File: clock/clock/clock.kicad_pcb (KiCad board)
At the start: 2 copper layers, 32.3 x 110 mm, 44 parts, among them J1 AVR-ISP, J10 Conn_01x07_Male, J11 CV_IN, J12 CLOCK_OUT, J13 SUBDIV_OUT, J2 EURORACK_CONN_10, J3 Conn_01x05_Female, J4 Conn_01x05_Male, J5 Conn_01x05_Female, J6 Conn_01x05_Male, J7 Conn_01x05_Female, J8 Conn_01x05_Male, J9 Conn_01x07_Female, SW1 SW_Push, SW2 SW_Push, SW3 Rotary_Encoder_Switch, U1 ATmega328P-PU, U2 L7805, U3 SM460281N, U4 SM460281N, U5 SM460281N, Y1 16MHz

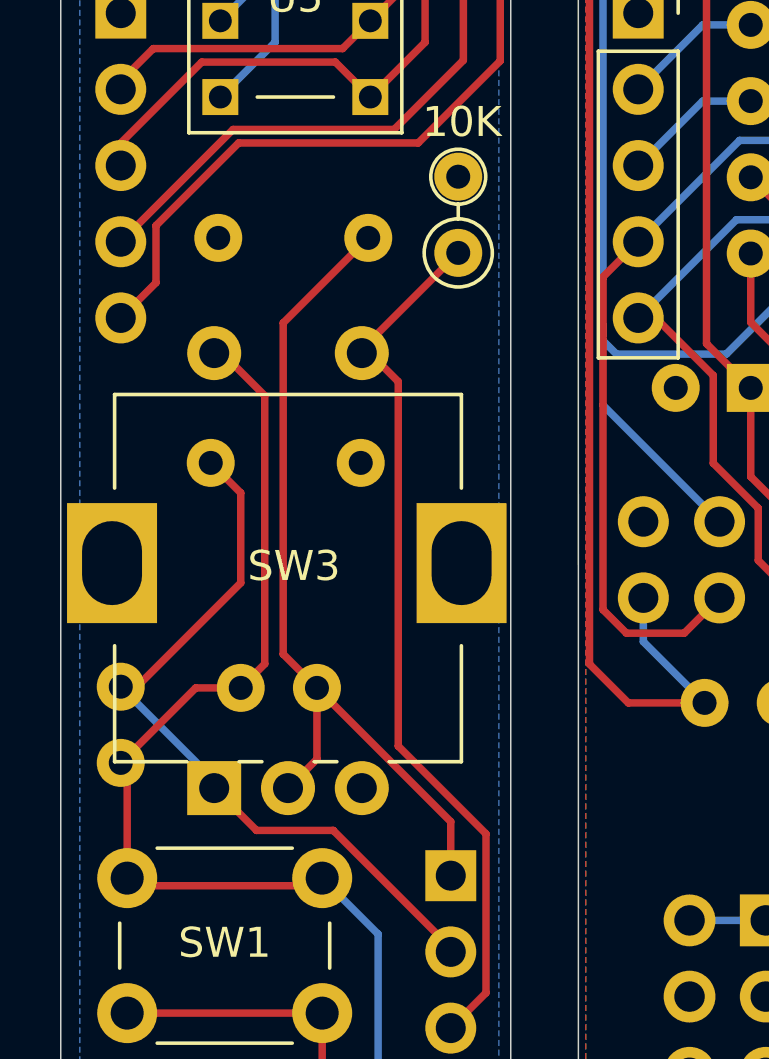
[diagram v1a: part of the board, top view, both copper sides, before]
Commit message: fix some PCB bugs
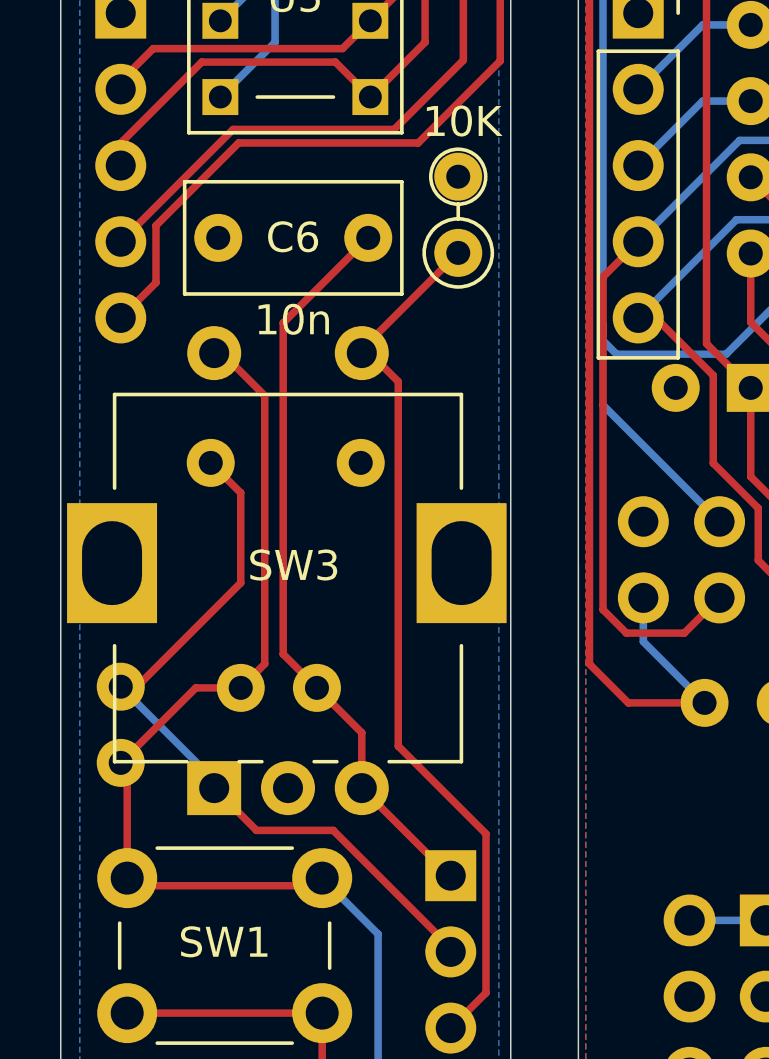
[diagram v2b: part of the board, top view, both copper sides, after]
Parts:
- C6: moved to F.Cu
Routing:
- net /KNOBR: track 28.5 -> 24.8 mm
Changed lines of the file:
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@@
+    )
+  )
+  (footprint "Capacitor_THT:C_Rect_L7.0mm_W3.5mm_P5.00mm" (layer "F.Cu")
+    (at 110.075 124.06 180)
+    (descr "C, Rect series, Radial, pin pitch=5.00mm, , length*width=7*3.5mm^2, Capacitor")
+    (tags "C Rect series Radial pin pitch 5.00mm  length 7mm width 3.5mm Capacitor")
+    (property "Sheetfile" "clock.kicad_sch")
+    (property "Sheetname" "")
+    (attr through_hole)
+    (fp_text reference "C6" (at 2.5 0) (layer "F.SilkS")
+      (effects (font (size 1 1) (thickness 0.15)))
+    )
+    (fp_text value "10n" (at 2.5 -2.75) (layer "F.SilkS")
+      (effects (font (size 1 1) (thickness 0.15)))
+    )
+    (fp_text user "${REFERENCE}" (at 2.5 0) (layer "F.Fab")
+      (effects (font (size 1 1) (thickness 0.15)))
+    )
+    (fp_line (start -1.12 -1.87) (end -1.12 1.87) (layer "F.SilkS") (width 0.12))
+    (fp_line (start -1.12 -1.87) (end 6.12 -1.87) (layer "F.SilkS") (width 0.12))
+    (fp_line (start -1.12 1.87) (end 6.12 1.87) (layer "F.SilkS") (width 0.12))
+    (fp_line (start 6.12 -1.87) (end 6.12 1.87) (layer "F.SilkS") (width 0.12))
+    (fp_line (start 6.25 -2) (end -1.25 -2) (layer "F.CrtYd") (width 0.05))
+    (fp_line (start -1.25 2) (end 6.25 2) (layer "F.CrtYd") (width 0.05))
+    (fp_line (start -1.25 -2) (end -1.25 2) (layer "F.CrtYd") (width 0.05))
+    (fp_line (start 6.25 2) (end 6.25 -2) (layer "F.CrtYd") (width 0.05))
+    (fp_line (start -1 -1.75) (end -1 1.75) (layer "F.Fab") (width 0.1))
+    (fp_line (start 6 1.75) (end 6 -1.75) (layer "F.Fab") (width 0.1))
+    (fp_line (start 6 -1.75) (end -1 -1.75) (layer "F.Fab") (width 0.1))
+    (fp_line (start -1 1.75) (end 6 1.75) (layer "F.Fab") (width 0.1))
+    (pad "1" thru_hole circle locked (at 0 0 180) (size 1.6 1.6) (drill 0.8) (layers *.Cu *.Mask)
+      (net 54 "/KNOBR") (pintype "passive"))
+    (pad "2" thru_hole circle locked (at 5 0 180) (size 1.6 1.6) (drill 0.8) (layers *.Cu *.Mask)
+      (net 25 "/AGND") (pintype "passive"))
+    (model "${KISYS3DMOD}/Capacitor_THT.3dshapes/C_Rect_L7.0mm_W3.5mm_P5.00mm.wrl"
+      (offset (xyz 0 0 0))
+      (scale (xyz 1 1 1))
+      (rotate (xyz 0 0 0))
     )
   )
@@
       (effects (font (size 1 1) (thickness 0.15)))
     )
+    (fp_line (start 10 3.28) (end 13.12 3.28) (layer "F.SilkS") (width 0.12))
+    (fp_line (start 10 -8.28) (end 13.12 -8.28) (layer "F.SilkS") (width 0.12))
     (fp_line (start 0.88 -4.129) (end 0.88 -3.37) (layer "F.SilkS") (width 0.12))
-    (fp_line (start 10 3.28) (end 13.12 3.28) (layer "F.SilkS") (width 0.12))
+    (fp_line (start 0.88 -8.28) (end 4.745 -8.28) (layer "F.SilkS") (width 0.12))
     (fp_line (start 13.12 -8.28) (end 13.12 3.28) (layer "F.SilkS") (width 0.12))
     (fp_line (start 0.88 -1.629) (end 0.88 -0.87) (layer "F.SilkS") (width 0.12))
-    (fp_line (start 10 -8.28) (end 13.12 -8.28) (layer "F.SilkS") (width 0.12))
-    (fp_line (start 0.88 -8.28) (end 0.88 -5.871) (layer "F.SilkS") (width 0.12))
-    (fp_line (start 0.88 -8.28) (end 4.745 -8.28) (layer "F.SilkS") (width 0.12))
     (fp_line (start 0.88 0.87) (end 0.88 3.28) (layer "F.SilkS") (width 0.12))
     (fp_line (start 0.88 3.28) (end 4.745 3.28) (layer "F.SilkS") (width 0.12))
+    (fp_line (start 0.88 -8.28) (end 0.88 -5.871) (layer "F.SilkS") (width 0.12))
     (fp_line (start 15.65 4.8) (end 15.65 -9.9) (layer "F.CrtYd") (width 0.05))
     (fp_line (start 15.65 -9.9) (end -1.15 -9.9) (layer "F.CrtYd") (width 0.05))
@@
     (fp_line (start -1.15 -9.9) (end -1.15 4.8) (layer "F.CrtYd") (width 0.05))
     (fp_line (start 13 3.87) (end 13 -8.87) (layer "F.Fab") (width 0.1))
+    (fp_line (start 1 3.87) (end 13 3.87) (layer "F.Fab") (width 0.1))
+    (fp_line (start 1 -8.87) (end 1 3.87) (layer "F.Fab") (width 0.1))
     (fp_line (start 13 -8.87) (end 1 -8.87) (layer "F.Fab") (width 0.1))
-    (fp_line (start 1 -8.87) (end 1 3.87) (layer "F.Fab") (width 0.1))
-    (fp_line (start 1 3.87) (end 13 3.87) (layer "F.Fab") (width 0.1))
     (fp_circle (center 7.5 -2.5) (end 10.5 -2.5) (layer "F.Fab") (width 0.1) (fill none))
     (pad "" thru_hole rect (at 7.5 3.285 90) (size 4 3) (drill oval 2.8 2) (layers *.Cu *.Mask))
@@
     (pad "1" thru_hole rect (at 0 -4.96 90) (size 1.8 1.8) (drill 1) (layers *.Cu *.Mask)
       (net 55 "/KNOBL") (pinfunction "A") (pintype "passive"))
-    (pad "2" thru_hole circle (at 0 -2.5 90) (size 1.8 1.8) (drill 1) (layers *.Cu *.Mask)
+    (pad "2" thru_hole circle (at 0 -0.04 90) (size 1.8 1.8) (drill 1) (layers *.Cu *.Mask)
       (net 54 "/KNOBR") (pinfunction "B") (pintype "passive"))
-    (pad "3" thru_hole circle (at 0 -0.04 90) (size 1.8 1.8) (drill 1) (layers *.Cu *.Mask)
+    (pad "3" thru_hole circle (at 0 -2.5 90) (size 1.8 1.8) (drill 1) (layers *.Cu *.Mask)
       (net 25 "/AGND") (pinfunction "C") (pintype "passive"))
     (pad "4" thru_hole circle (at 14.5 -4.96 90) (size 1.8 1.8) (drill 1) (layers *.Cu *.Mask)
@@
       (net 25 "/AGND") (pintype "passive"))
     (model "${KICAD6_3DMODEL_DIR}/Resistor_THT.3dshapes/R_Axial_DIN0207_L6.3mm_D2.5mm_P2.54mm_Vertical.wrl"
-      (offset (xyz 0 0 0))
-      (scale (xyz 1 1 1))
-      (rotate (xyz 0 0 0))
-    )
-  )
-  (footprint "Capacitor_THT:C_Rect_L7.0mm_W3.5mm_P5.00mm" (layer "B.Cu")
-    (at 110.075 124.06 180)
-    (descr "C, Rect series, Radial, pin pitch=5.00mm, , length*width=7*3.5mm^2, Capacitor")
-    (tags "C Rect series Radial pin pitch 5.00mm  length 7mm width 3.5mm Capacitor")
-    (property "Sheetfile" "clock.kicad_sch")
-    (property "Sheetname" "")
-    (attr through_hole)
-    (fp_text reference "C6" (at 2.5 0 180) (layer "B.SilkS")
-      (effects (font (size 1 1) (thickness 0.15)) (justify mirror))
-    )
-    (fp_text value "10n" (at 2.5 2.75 180) (layer "B.SilkS")
-      (effects (font (size 1 1) (thickness 0.15)) (justify mirror))
-    )
-    (fp_text user "${REFERENCE}" (at 2.5 0 180) (layer "B.Fab")
-      (effects (font (size 1 1) (thickness 0.15)) (justify mirror))
-    )
-    (fp_line (start -1.12 1.87) (end -1.12 -1.87) (layer "B.SilkS") (width 0.12))
-    (fp_line (start -1.12 1.87) (end 6.12 1.87) (layer "B.SilkS") (width 0.12))
-    (fp_line (start -1.12 -1.87) (end 6.12 -1.87) (layer "B.SilkS") (width 0.12))
-    (fp_line (start 6.12 1.87) (end 6.12 -1.87) (layer "B.SilkS") (width 0.12))
-    (fp_line (start 6.25 2) (end -1.25 2) (layer "B.CrtYd") (width 0.05))
-    (fp_line (start -1.25 -2) (end 6.25 -2) (layer "B.CrtYd") (width 0.05))
-    (fp_line (start -1.25 2) (end -1.25 -2) (layer "B.CrtYd") (width 0.05))
-    (fp_line (start 6.25 -2) (end 6.25 2) (layer "B.CrtYd") (width 0.05))
-    (fp_line (start -1 1.75) (end -1 -1.75) (layer "B.Fab") (width 0.1))
-    (fp_line (start 6 -1.75) (end 6 1.75) (layer "B.Fab") (width 0.1))
-    (fp_line (start 6 1.75) (end -1 1.75) (layer "B.Fab") (width 0.1))
-    (fp_line (start -1 -1.75) (end 6 -1.75) (layer "B.Fab") (width 0.1))
-    (pad "1" thru_hole circle locked (at 0 0 180) (size 1.6 1.6) (drill 0.8) (layers *.Cu *.Mask)
-      (net 54 "/KNOBR") (pintype "passive"))
-    (pad "2" thru_hole circle locked (at 5 0 180) (size 1.6 1.6) (drill 0.8) (layers *.Cu *.Mask)
-      (net 25 "/AGND") (pintype "passive"))
-    (model "${KISYS3DMOD}/Capacitor_THT.3dshapes/C_Rect_L7.0mm_W3.5mm_P5.00mm.wrl"
       (offset (xyz 0 0 0))
       (scale (xyz 1 1 1))
@@
   (segment (start 124.400011 129.998601) (end 124.400011 123.615011) (width 0.25) (layer "F.Cu") (net 53))
   (segment (start 124.400011 123.615011) (end 122.825 122.04) (width 0.25) (layer "F.Cu") (net 53))
+  (segment (start 112.78 145.32) (end 109.86 142.4) (width 0.25) (layer "F.Cu") (net 54))
   (segment (start 108.365 139.06) (end 107.239999 137.934999) (width 0.25) (layer "F.Cu") (net 54))
   (segment (start 107.239999 137.934999) (end 107.239999 126.895001) (width 0.25) (layer "F.Cu") (net 54))
-  (segment (start 112.825 143.52) (end 112.825 145.32) (width 0.25) (layer "F.Cu") (net 54))
-  (segment (start 108.365 141.435) (end 107.4 142.4) (width 0.25) (layer "F.Cu") (net 54))
+  (segment (start 109.86 142.4) (end 109.86 140.555) (width 0.25) (layer "F.Cu") (net 54))
   (segment (start 107.239999 126.895001) (end 110.075 124.06) (width 0.25) (layer "F.Cu") (net 54))
-  (segment (start 108.365 139.06) (end 108.365 141.435) (width 0.25) (layer "F.Cu") (net 54))
-  (segment (start 112.825 143.52) (end 108.365 139.06) (width 0.25) (layer "F.Cu") (net 54))
+  (segment (start 112.825 145.32) (end 112.78 145.32) (width 0.25) (layer "F.Cu") (net 54))
+  (segment (start 109.86 140.555) (end 108.365 139.06) (width 0.25) (layer "F.Cu") (net 54))
   (segment (start 102.365 139.02) (end 101.825 139.02) (width 0.25) (layer "F.Cu") (net 55))
   (segment (start 112.825 147.724998) (end 108.910002 143.81) (width 0.25) (layer "F.Cu") (net 55))

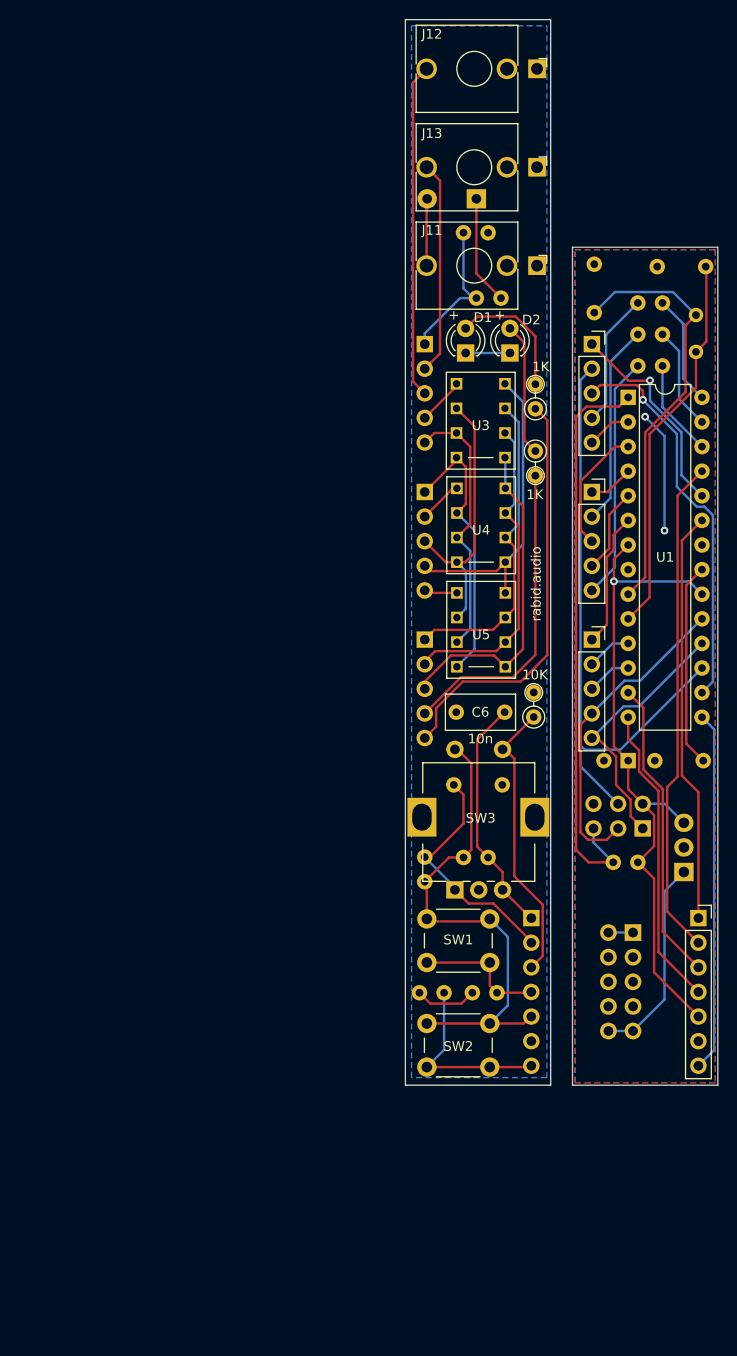
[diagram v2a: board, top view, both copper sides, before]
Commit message: re-create panel in kicad
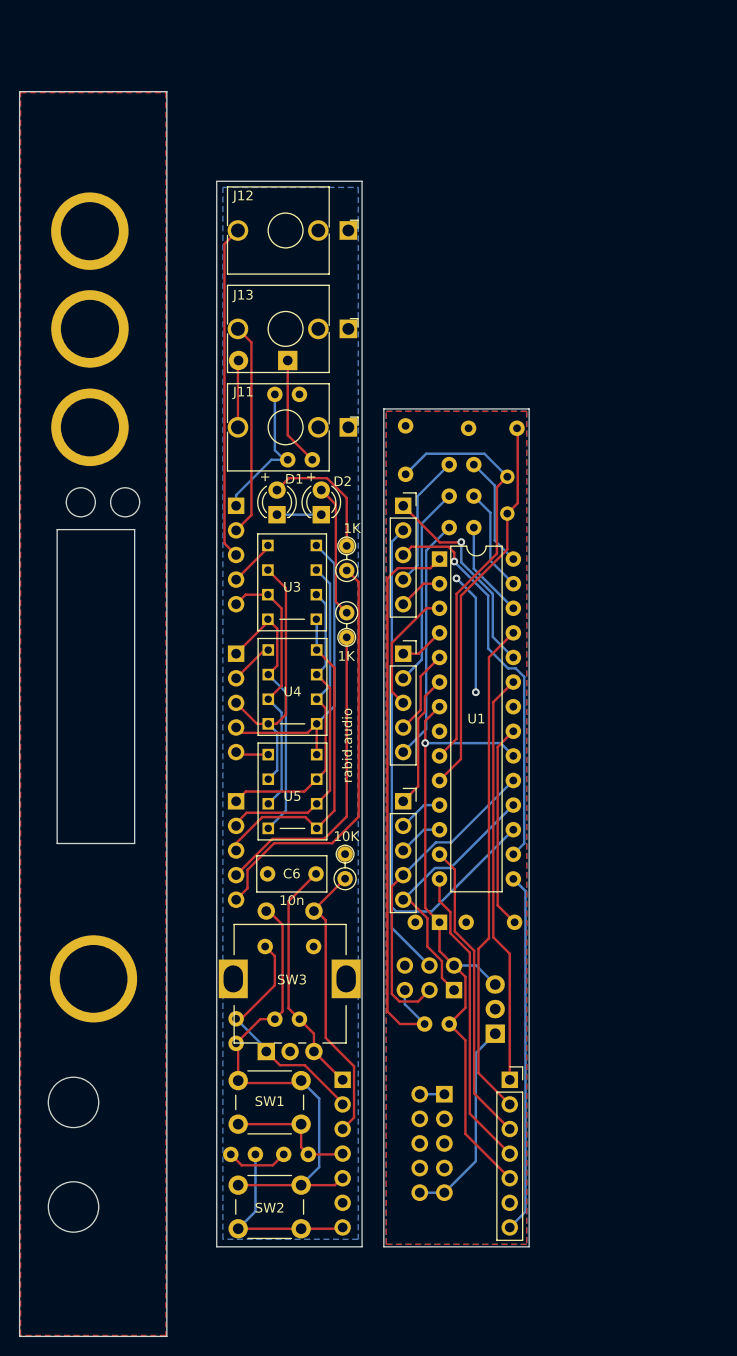
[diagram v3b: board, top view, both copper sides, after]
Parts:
- added HJ1: thonkiconn-hole, synth:thonkiconn_hole, F.Cu at (67.3, 94.7)
- added HJ1: thonkiconn-hole, synth:thonkiconn_hole, F.Cu at (67.3, 84.5)
- added HJ1: thonkiconn-hole, synth:thonkiconn_hole, F.Cu at (67.2, 74.4)
- added REF**: 3mm_led_hole, synth:3mm_led_hole, F.Cu at (66.3, 102.4)
- added REF**: eurorack_screw_hole, synth:eurorack_screw_hole, F.Cu at (67.5, 185.5)
- added REF**: eurorack_screw_hole, synth:eurorack_screw_hole, F.Cu at (67.5, 63.0)
- added REF**: knob_hole, synth:knob_hole, F.Cu at (67.6, 151.6)
- added REF**: toggle_sw_hole, synth:toggle_sw_hole, F.Cu at (65.6, 164.3)
- added REF**: toggle_sw_hole, synth:toggle_sw_hole, F.Cu at (65.6, 175.1)
- added REF**: 3mm_led_hole, synth:3mm_led_hole, F.Cu at (70.9, 102.4)
- moved J11 25.6 mm to (93.9, 94.7)
- moved J7 25.6 mm to (99.6, 133.3)
- moved J8 25.6 mm to (82.3, 133.3)
- moved R2 25.6 mm to (93.8, 109.4)
- moved R3 25.6 mm to (93.8, 113.8)
- moved R4 25.6 mm to (89.8, 169.7)
- moved R5 25.6 mm to (84.3, 169.7)
- moved C1 25.6 mm to (103.3, 145.8)
- moved C2 25.6 mm to (106.1, 145.8)
- moved C3 25.6 mm to (99.8, 94.5)
- moved C4 25.6 mm to (106.3, 94.8)
- moved C5 25.6 mm to (85.3, 148.2)
- moved C6 25.6 mm to (90.6, 140.8)
- moved D1 25.6 mm to (86.6, 103.7)
- moved D2 25.6 mm to (91.1, 103.7)
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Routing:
- added copper zone on F.Cu, net (none)
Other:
- board size 32.3 x 110 mm -> 52.6 x 128.5 mm

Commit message: graphics
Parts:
- moved D2 60.0 mm to (151.1, 103.7)
- moved R2 60.0 mm to (153.8, 109.4)
- moved R3 60.0 mm to (153.8, 113.8)
- moved SW3 60.0 mm to (150.4, 159.1)
- moved C1 60.0 mm to (163.3, 145.8)
- moved C2 60.0 mm to (166.1, 145.8)
- moved C3 60.0 mm to (159.8, 94.5)
- moved C4 60.0 mm to (166.3, 94.8)
- moved C5 60.0 mm to (145.3, 148.2)
- moved C6 60.0 mm to (150.6, 140.8)
- moved D1 60.0 mm to (146.6, 103.7)
- moved D3 60.0 mm to (147.7, 87.8)
- moved J1 60.0 mm to (164.8, 152.8)
- moved J10 60.0 mm to (153.3, 162.0)
- moved J11 60.0 mm to (153.9, 94.7)
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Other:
- board size 52.6 x 128.5 mm -> 112.6 x 128.5 mm
- board text added: "2023-02-03 REV. B"
- board text removed: "2023-01-01 REV. A"
